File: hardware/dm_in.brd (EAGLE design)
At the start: 76.5 x 50.8 mm, 56 parts, among them IC102 MAX487CSA, IC2 LTV-356T, IC3 78SO05, IC4 LTV-354T, IC6 ATMEGA328-A, X1 AKL_183-02, X2 AKL_183-02, X3 AKL_183-04, X4 AKL_183-02, X5 AKL_183-02, X6 AKL_183-02, X7 AKL_183-02

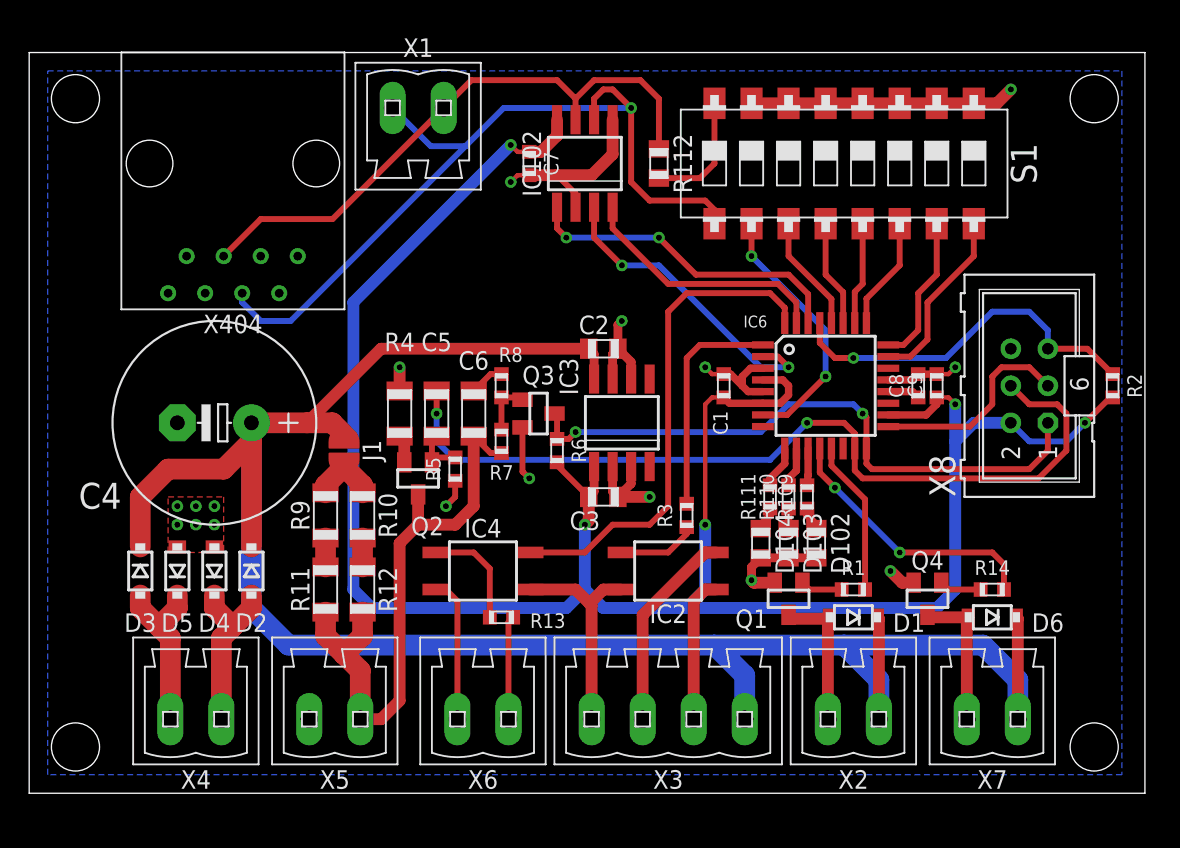
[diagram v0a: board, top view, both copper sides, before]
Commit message: Detailverbesserungen an Türmodul
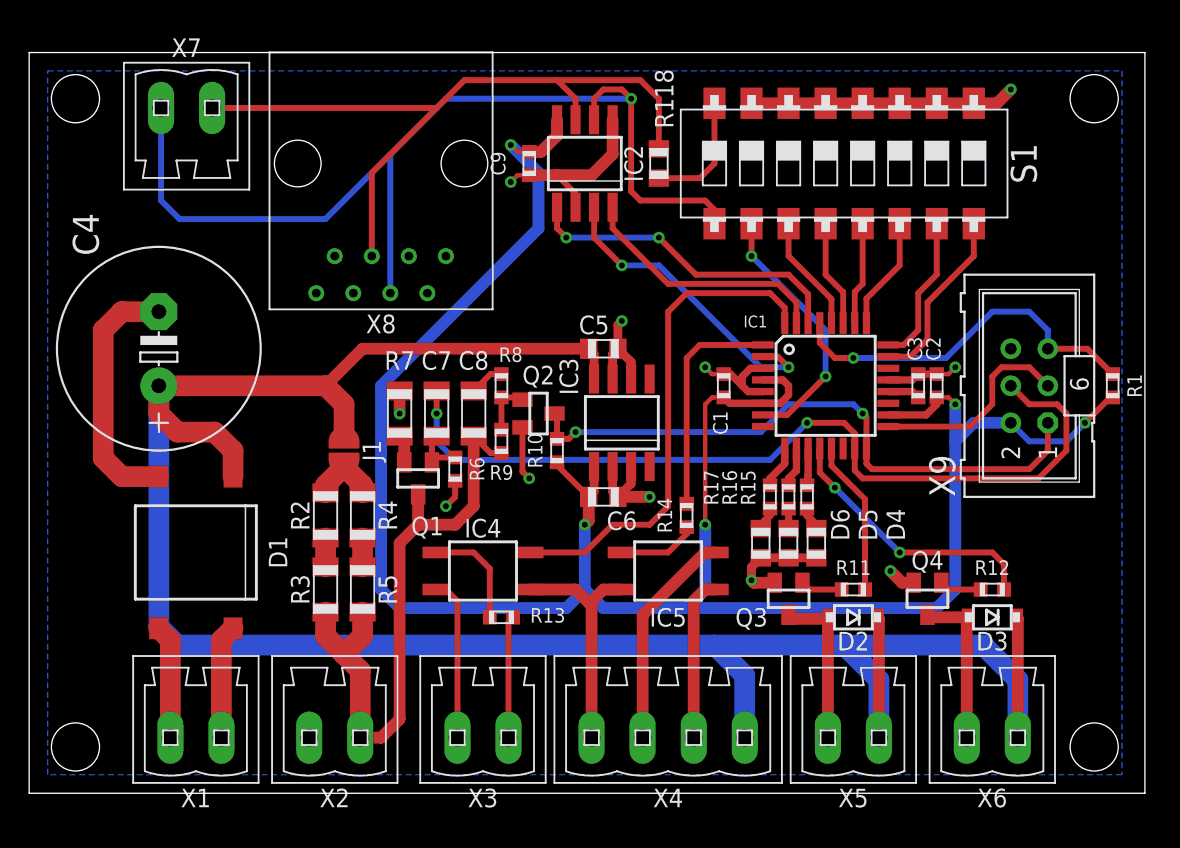
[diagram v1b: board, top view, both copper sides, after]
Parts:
- removed D102: GN, led:CHIP_0805
- removed D103: GE, led:CHIP_0805
- removed D104: RT, led:CHIP_0805
- removed IC102: MAX487CSA, ic-wandler:SOP08_127
- removed X404: (no value), stecker:C-BMJ-0102
- added IC5: LTV-356T, ic-optokoppler:SOP04_254
- added X9: (no value), stecker:ML6
- C2: value 330nF -> 100nF; device passiv:CHIP_0805 -> passiv:CHIP_0603
- C3: device passiv:CHIP_0805 -> passiv:CHIP_0603
- C4: value (none) -> 470μF 50V
- C5: value 1μF -> 330nF; device passiv:CHIP_1206 -> passiv:CHIP_0805
- C6: value 1μF -> 100nF; device passiv:CHIP_1206 -> passiv:CHIP_0805
- C7, C8: value 100nF -> 1μF; device passiv:CHIP_0603 -> passiv:CHIP_1206
- D1: device diode:SOD123 -> diode:SDIP04_508
- D4: value (none) -> GN; device diode:SOD123 -> led:CHIP_0805
- D5: value (none) -> GE; device diode:SOD123 -> led:CHIP_0805
- D6: value (none) -> RT; device diode:SOD123 -> led:CHIP_0805
- IC2: value LTV-356T -> MAX487CSA; device ic-optokoppler:SOP04_254 -> ic-wandler:SOP08_127
- Q1, Q2: value (none) -> BC337
- R1: value (none) -> 10kΩ
- R10: value 10Ω -> 10kΩ; device passiv:CHIP_1206 -> passiv:CHIP_0603
- R11, R12: value 10Ω -> 1kΩ; device passiv:CHIP_1206 -> passiv:CHIP_0603
- R13: value (none) -> 2,2kΩ
- R14: value (none) -> 330Ω
- R2, R3: value (none) -> 10Ω; device passiv:CHIP_0603 -> passiv:CHIP_1206
- R5: value 10kΩ -> 10Ω; device passiv:CHIP_0603 -> passiv:CHIP_1206
- R7: value 47kΩ -> 10Ω; device passiv:CHIP_0603 -> passiv:CHIP_1206
- R9: value 10Ω -> 47kΩ; device passiv:CHIP_1206 -> passiv:CHIP_0603
- X3: value AKL_183-04 -> AKL_183-02; device anschluss:AKL_183-04 -> anschluss:AKL_183-02
- X4: value AKL_183-02 -> AKL_183-04; device anschluss:AKL_183-02 -> anschluss:AKL_183-04
- X8: device stecker:ML6 -> stecker:C-BMJ-0102
- moved X7 69.3 mm to (10.8, 47.0), turned to 0 degrees
- moved D3 58.5 mm to (66.0, 12.1), turned to 180 degrees
- moved R2 54.7 mm to (20.3, 19.1)
- moved X8 47.0 mm to (24.1, 43.2), turned to 180 degrees
- moved X1 45.8 mm to (11.4, 3.81), turned to 180 degrees
- moved D1 45.3 mm to (11.4, 16.5)
- moved R12 43.2 mm to (66.0, 14.0), turned to 180 degrees
- moved D5 42.0 mm to (52.1, 17.1), turned to 270 degrees
- moved D2 41.4 mm to (56.5, 12.1), turned to 180 degrees
- moved D4 41.3 mm to (54.0, 17.1), turned to 270 degrees
- moved R11 36.2 mm to (56.5, 14.0), turned to 180 degrees
- moved X2 35.6 mm to (21.0, 3.81)
- moved X5 35.6 mm to (56.5, 3.81)
- moved X6 34.9 mm to (66.0, 3.81)
- moved X4 32.4 mm to (43.8, 3.81)
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- renumbered IC6 to IC1, R109 to R15, R110 to R16, R111 to R17, R112 to R118
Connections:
- net +5V: now also C2.1, C6.1, IC2.8, R1.2, R10.2, X9.2; no longer C3.1, C7.1, IC102.8, R2.2, R6.2, X8.2
- net GND: now also C5.2, C6.2, D1.2, D4.2, D5.2, D6.2, IC2.5, IC5.2, Q2.2, R6.1, R7.1, X2.2, X4.4, X9.6; no longer C7.2, C8.2, D102.2, D103.2, D104.2, D4.A, D5.A, IC102.2, IC102.5, Q1.2, R4.1, R5.1, X3.4, X5.2, X8.6
- net N$10: now also R14.1; no longer R3.1
- net N$11: now also IC5.1, R14.2; no longer IC2.1, R3.2
- net N$12: now also R2.1, R4.1; no longer R10.1, R9.1
- net N$13: now also R2.2, R3.1; no longer R11.1, R9.2
- net N$14: now also X3.1; no longer X6.1
- net N$16: now also Q1.2, R7.2; no longer Q2.2, R4.2
- net N$17: now also C7.2, Q1.1, R6.2; no longer C5.2, Q2.1, R5.2
- net N$18: now also Q2.1, R9.1; no longer Q3.1, R7.1
- net N$19: now also C8.2; no longer C6.2
- net N$2: now also X3.2; no longer X6.2
- net N$20: now also D1.4, X1.1; no longer D2.A, D4.K, X4.1
- net N$21: now also C8.1, Q1.3, R3.2, R5.2, R9.2, X2.1; no longer C6.1, Q2.3, R11.2, R12.2, R7.2, X5.1
- net N$22: now also D1.3, X1.2; no longer D3.A, D5.K, X4.2
- net N$23: now also R4.2, R5.1; no longer R10.2, R12.1
- net N$24: now also R12.2; no longer R14.2
- net N$25: now also D3.A, X6.2; no longer D6.A, X7.2
- net N$26: now also R12.1; no longer R14.1
- net N$27: now also IC2.7, X7.2, X8.P$5; no longer IC102.7, X1.2, X404.P$5
- net N$3: now also IC2.6, X7.1, X8.P$4; no longer IC102.6, X1.1, X404.P$4
- net N$36: now also D6.1; no longer D104.1
- net N$38: now also X9.3; no longer X8.3
- net N$39: now also C3.1; no longer C8.1
- net N$4: now also R1.1, X9.5; no longer R2.1, X8.5
- net N$5: now also R11.1; no longer R1.1
- net N$6: now also Q3.1, R11.2; no longer Q1.1, R1.2
- net N$62: now also D4.1; no longer D102.1
- net N$63: now also D5.1; no longer D103.1
- net N$7: now also D2.A, Q3.3, X5.2; no longer D1.A, Q1.3, X2.2
- net N$8: now also IC5.3, X4.2; no longer IC2.3, X3.2
- net N$9: now also IC5.4, X4.3; no longer IC2.4, X3.3
- net RX: now also IC2.1; no longer IC102.1
- net RX2: now also Q2.3, R10.1, X9.1; no longer Q3.3, R6.1, X8.1
- net TE: now also IC2.3; no longer IC102.3
- net TX: now also IC2.4; no longer IC102.4
- net TX2: now also C7.1, X9.4; no longer C5.1, X8.4
- net VCC: now also C5.1, D1.1, X4.1, X5.1, X6.1; no longer C2.1, D1.K, D6.K, X2.1, X3.1, X7.1
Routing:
- net GND: track 88.0 -> 106.6 mm, vias 17 -> 11
- net N$3: track 57.3 -> 70.3 mm
- net VCC: track 147.5 -> 158.5 mm
- net N$27: track 41.3 -> 50.6 mm
- net N$22: track 12.0 -> 7.83 mm
- net N$20: track 12.0 -> 7.83 mm
- net N$21: track 41.2 -> 43.7 mm
- net N$9: track 13.9 -> 15.2 mm
- net N$8: track 9.93 -> 11.2 mm
- net N$7: track 9.83 -> 11.1 mm
- net N$25: track 9.89 -> 11.2 mm
- net N$2: track 9.93 -> 11.2 mm
- net N$14: track 7.12 -> 8.39 mm
- net +5V: track 150.2 -> 149.1 mm
- removed copper zone on layer 1, net GND

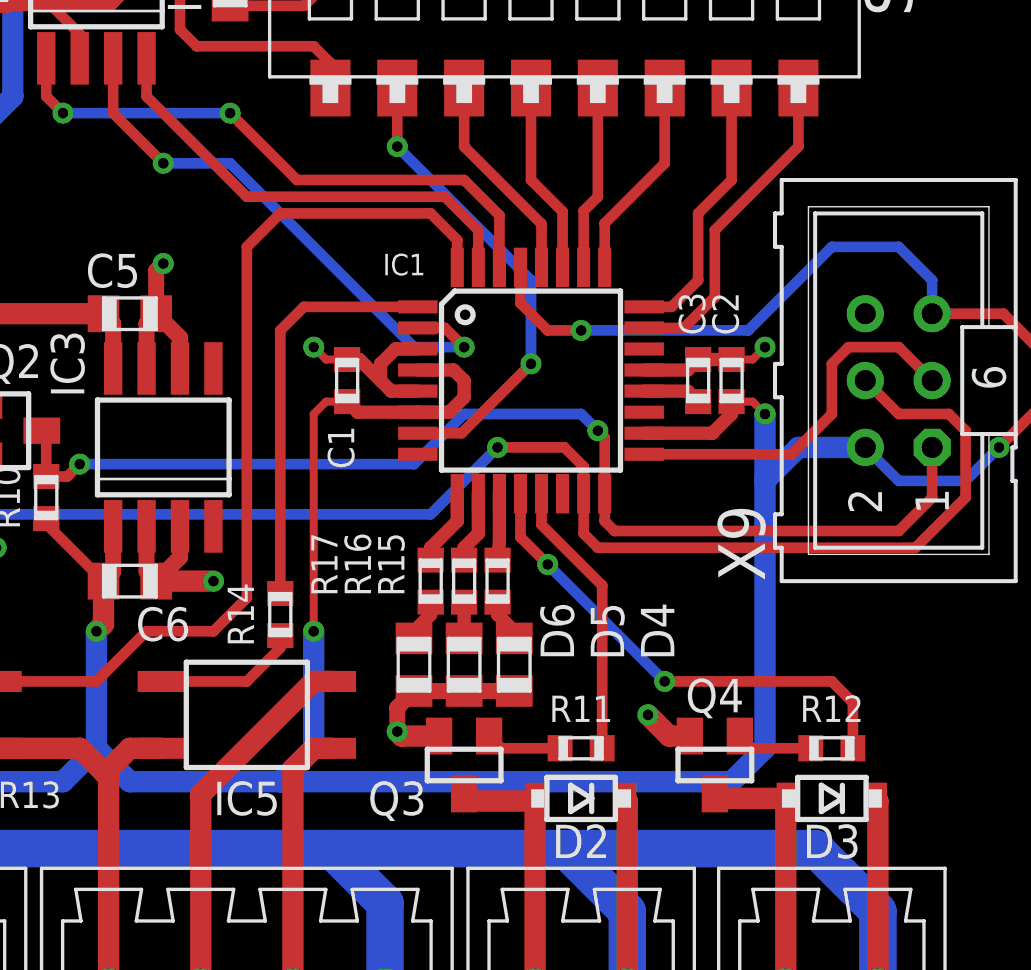
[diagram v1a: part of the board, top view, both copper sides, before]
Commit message: Minimale Layoutverbesserung im Türmodul
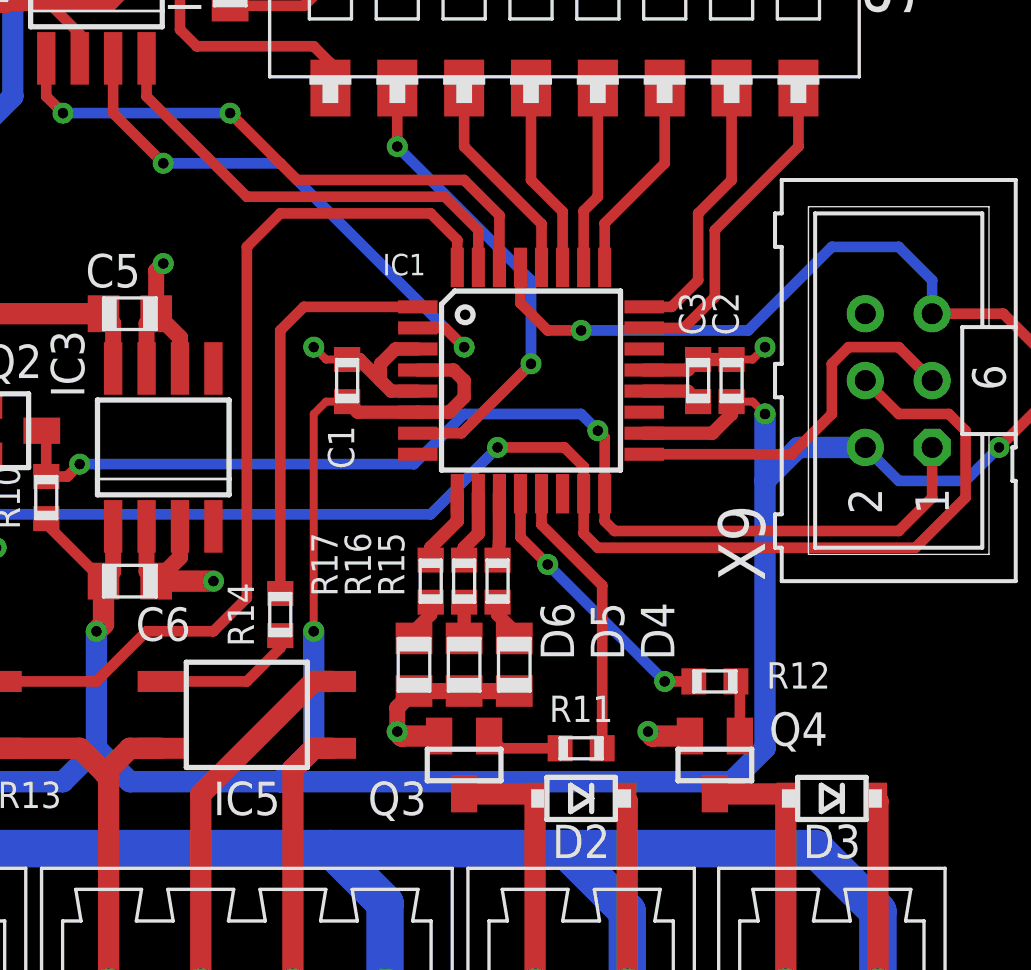
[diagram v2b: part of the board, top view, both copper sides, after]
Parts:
- moved R12 5.12 mm to (61.6, 16.5), turned to 0 degrees
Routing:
- net N$26: track 18.6 -> 10.5 mm
- net N$24: track 2.89 -> 2.14 mm
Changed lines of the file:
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@@
 </element>
 <element name="Q4" library="transistor" package="SOT23" value="" x="61.595" y="13.335" smashed="yes" rot="R180">
-<attribute name="NAME" x="61.595" y="15.335" size="1.27" layer="25" align="bottom-center"/>
+<attribute name="NAME" x="64.77" y="14.065" size="1.27" layer="25" align="bottom-center"/>
 <attribute name="VALUE" x="61.595" y="15.335" size="1.27" layer="27" rot="R180" align="top-center"/>
 </element>
-<element name="R12" library="passiv" package="CHIP_0603" value="1kΩ" x="66.04" y="13.97" smashed="yes" rot="R180">
-<attribute name="NAME" x="66.04" y="14.97" size="1" layer="25" align="bottom-center"/>
-<attribute name="VALUE" x="66.04" y="14.97" size="1" layer="27" rot="R180" align="top-center"/>
+<element name="R12" library="passiv" package="CHIP_0603" value="1kΩ" x="61.595" y="16.51" smashed="yes">
+<attribute name="NAME" x="64.77" y="16.24" size="1" layer="25" align="bottom-center"/>
+<attribute name="VALUE" x="61.595" y="15.51" size="1" layer="27" align="top-center"/>
 </element>
 <element name="D3" library="diode" package="SOD123" value="" x="66.04" y="12.065" smashed="yes" rot="R180">
@@
 <wire x1="38.735" y1="20.685" x2="38.37" y2="20.32" width="0.6096" layer="1"/>
 <wire x1="36.195" y1="22.695" x2="36.195" y2="22.495" width="0.4064" layer="1"/>
-<wire x1="36.195" y1="22.495" x2="38.37" y2="20.32" width="0.4064" layer="1"/>
 <contactref element="X9" pad="2"/>
 <contactref element="IC1" pad="18"/>
@@
 <wire x1="52.07" y1="27.94" x2="51.67" y2="28.34" width="0.508" layer="1"/>
 <wire x1="51.67" y1="28.34" x2="50.31" y2="28.34" width="0.508" layer="1"/>
-<wire x1="38.37" y1="20.32" x2="38.37" y2="18.685" width="0.8128" layer="1"/>
 <wire x1="38.37" y1="18.685" x2="38.1" y2="18.415" width="0.8128" layer="1"/>
 <via x="38.1" y="18.415" extent="1-16" drill="0.4"/>
@@
 <wire x1="34.925" y1="38.735" x2="34.925" y2="42.545" width="0.8128" layer="16"/>
 <wire x1="34.925" y1="42.545" x2="33.02" y2="44.45" width="0.8128" layer="16"/>
+<wire x1="38.37" y1="20.32" x2="38.37" y2="18.685" width="0.8128" layer="1"/>
+<wire x1="36.195" y1="22.495" x2="38.37" y2="20.32" width="0.4064" layer="1"/>
 </signal>
 <signal name="GND">
@@
 <wire x1="51.12" y1="14.435" x2="49.7" y2="14.435" width="0.8128" layer="1"/>
 <wire x1="49.7" y1="14.435" x2="49.53" y2="14.605" width="0.8128" layer="1"/>
-<wire x1="60.645" y1="14.435" x2="59.86" y2="14.435" width="0.8128" layer="1"/>
-<wire x1="59.86" y1="14.435" x2="59.055" y2="15.24" width="0.8128" layer="1"/>
+<wire x1="60.645" y1="14.435" x2="59.225" y2="14.435" width="0.8128" layer="1"/>
+<wire x1="59.225" y1="14.435" x2="59.055" y2="14.605" width="0.8128" layer="1"/>
 <via x="49.53" y="14.605" extent="1-16" drill="0.4"/>
-<via x="59.055" y="15.24" extent="1-16" drill="0.4"/>
+<via x="59.055" y="14.605" extent="1-16" drill="0.4"/>
 <contactref element="X9" pad="6"/>
 <contactref element="X9" pad="6"/>
@@
 <wire x1="33.49" y1="42.38" x2="33.02" y2="41.91" width="0.3048" layer="1"/>
 <via x="33.02" y="41.91" extent="1-16" drill="0.4"/>
-<wire x1="40.37" y1="20.32" x2="42.545" y2="20.32" width="0.8128" layer="1"/>
 <wire x1="50.31" y1="27.54" x2="49.295" y2="27.54" width="0.508" layer="1"/>
 <wire x1="49.295" y1="27.54" x2="48.895" y2="27.94" width="0.508" layer="1"/>
@@
 <wire x1="5.08" y1="31.75" x2="6.35" y2="33.02" width="1.4224" layer="1"/>
 <wire x1="6.35" y1="33.02" x2="8.89" y2="33.02" width="1.4224" layer="1"/>
+<wire x1="40.37" y1="20.32" x2="42.545" y2="20.32" width="0.8128" layer="1"/>
 </signal>
 <signal name="N$6">
@@
 <contactref element="D2" pad="A"/>
 <contactref element="X5" pad="2"/>
+<wire x1="52.07" y1="12.235" x2="54.695" y2="12.235" width="0.8128" layer="1"/>
+<wire x1="54.695" y1="12.235" x2="54.865" y2="12.065" width="0.8128" layer="1"/>
 <wire x1="54.765" y1="3.81" x2="54.765" y2="11.965" width="0.8128" layer="1"/>
 <wire x1="54.765" y1="11.965" x2="54.865" y2="12.065" width="0.8128" layer="1"/>
-<wire x1="54.765" y1="11.965" x2="52.34" y2="11.965" width="0.8128" layer="1"/>
-<wire x1="52.34" y1="11.965" x2="52.07" y2="12.235" width="0.8128" layer="1"/>
 </signal>
 <signal name="VCC">
@@
 <contactref element="R12" pad="2"/>
 <contactref element="Q4" pad="1"/>
-<wire x1="65.24" y1="13.97" x2="63.01" y2="13.97" width="0.4064" layer="1"/>
-<wire x1="63.01" y1="13.97" x2="62.545" y2="14.435" width="0.4064" layer="1"/>
+<wire x1="62.545" y1="14.435" x2="62.545" y2="16.36" width="0.4064" layer="1"/>
+<wire x1="62.545" y1="16.36" x2="62.395" y2="16.51" width="0.4064" layer="1"/>
 </signal>
 <signal name="N$25">
@@
 <contactref element="D3" pad="A"/>
 <contactref element="X6" pad="2"/>
-<wire x1="64.39" y1="12.065" x2="61.765" y2="12.065" width="0.8128" layer="1"/>
-<wire x1="61.765" y1="12.065" x2="61.595" y2="12.235" width="0.8128" layer="1"/>
 <wire x1="64.29" y1="3.81" x2="64.29" y2="11.965" width="0.8128" layer="1"/>
 <wire x1="64.29" y1="11.965" x2="64.39" y2="12.065" width="0.8128" layer="1"/>
+<wire x1="61.595" y1="12.235" x2="64.22" y2="12.235" width="0.8128" layer="1"/>
+<wire x1="64.22" y1="12.235" x2="64.39" y2="12.065" width="0.8128" layer="1"/>
 </signal>
 <signal name="N$26">
@@
 <wire x1="55.245" y1="20.955" x2="59.69" y2="16.51" width="0.4064" layer="16"/>
 <via x="59.69" y="16.51" extent="1-16" drill="0.4"/>
-<wire x1="59.69" y1="16.51" x2="66.04" y2="16.51" width="0.4064" layer="1"/>
-<wire x1="66.04" y1="16.51" x2="66.84" y2="15.71" width="0.4064" layer="1"/>
-<wire x1="66.84" y1="15.71" x2="66.84" y2="13.97" width="0.4064" layer="1"/>
+<wire x1="60.795" y1="16.51" x2="59.69" y2="16.51" width="0.4064" layer="1"/>
 </signal>
 <signal name="TE">
@@
 <wire x1="51.34" y1="29.94" x2="52.07" y2="29.21" width="0.4064" layer="1"/>
 <via x="52.07" y="29.21" extent="1-16" drill="0.4"/>
-<wire x1="52.07" y1="29.21" x2="50.165" y2="29.21" width="0.4064" layer="16"/>
-<wire x1="50.165" y1="29.21" x2="43.18" y2="36.195" width="0.4064" layer="16"/>
-<wire x1="43.18" y1="36.195" x2="40.64" y2="36.195" width="0.4064" layer="16"/>
+<wire x1="52.07" y1="29.21" x2="45.085" y2="36.195" width="0.4064" layer="16"/>
+<wire x1="45.085" y1="36.195" x2="40.64" y2="36.195" width="0.4064" layer="16"/>
 <via x="40.64" y="36.195" extent="1-16" drill="0.4"/>
 <wire x1="40.64" y1="36.195" x2="38.735" y2="38.1" width="0.4064" layer="1"/>
